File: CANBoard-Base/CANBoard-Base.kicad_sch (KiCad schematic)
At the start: 9 parts, among them J1 DTM12 A, J2 DTM12 B, U1 CANBoard, U8 LD1117S33CTR

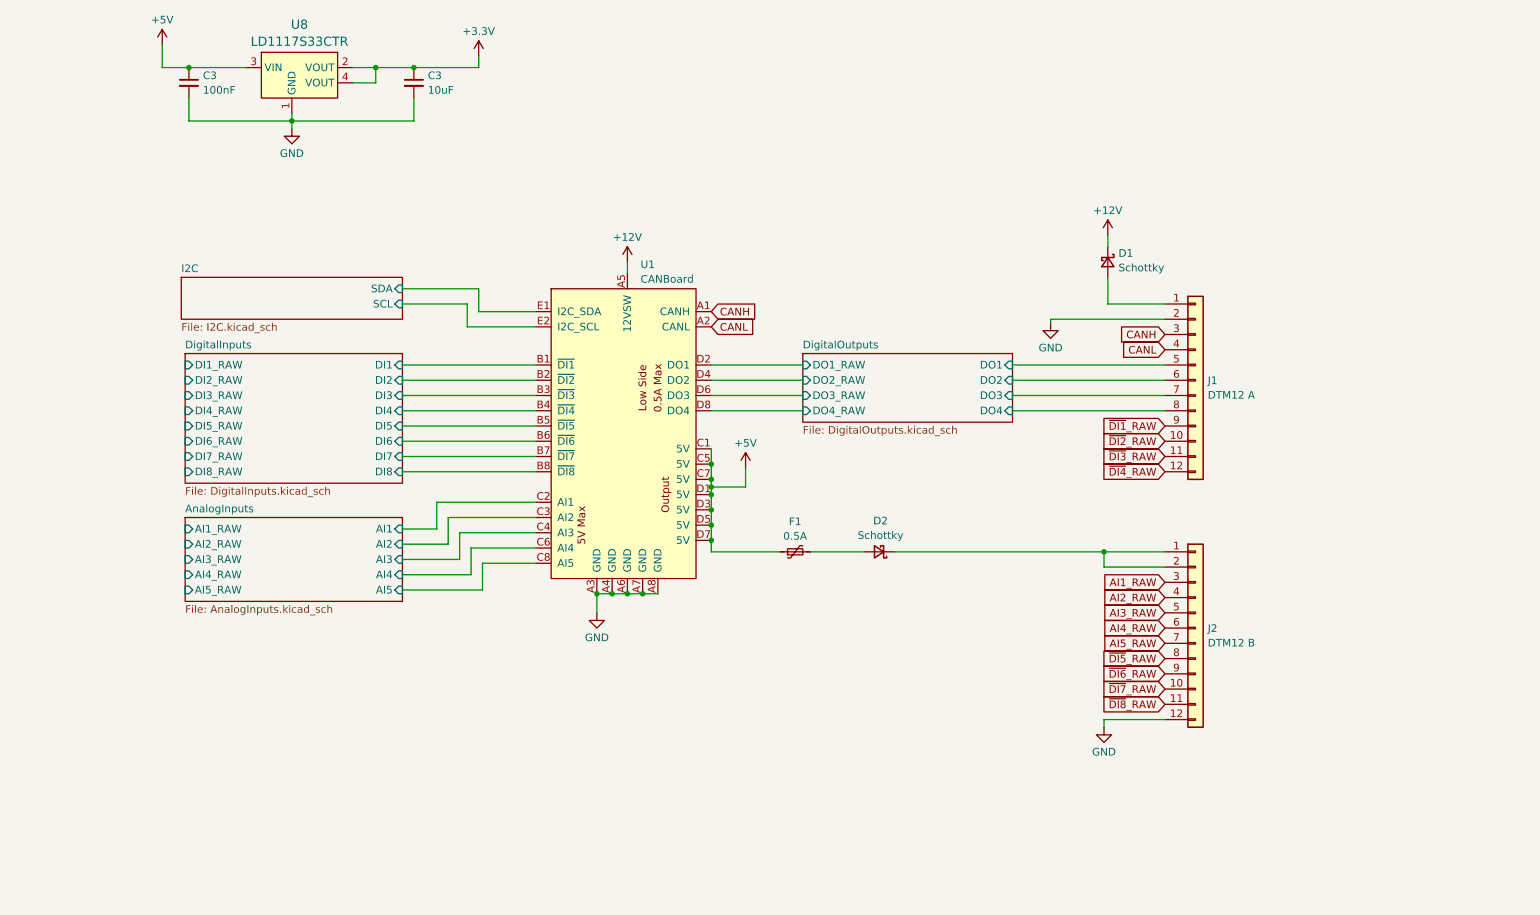
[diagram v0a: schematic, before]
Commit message: Switched to v2
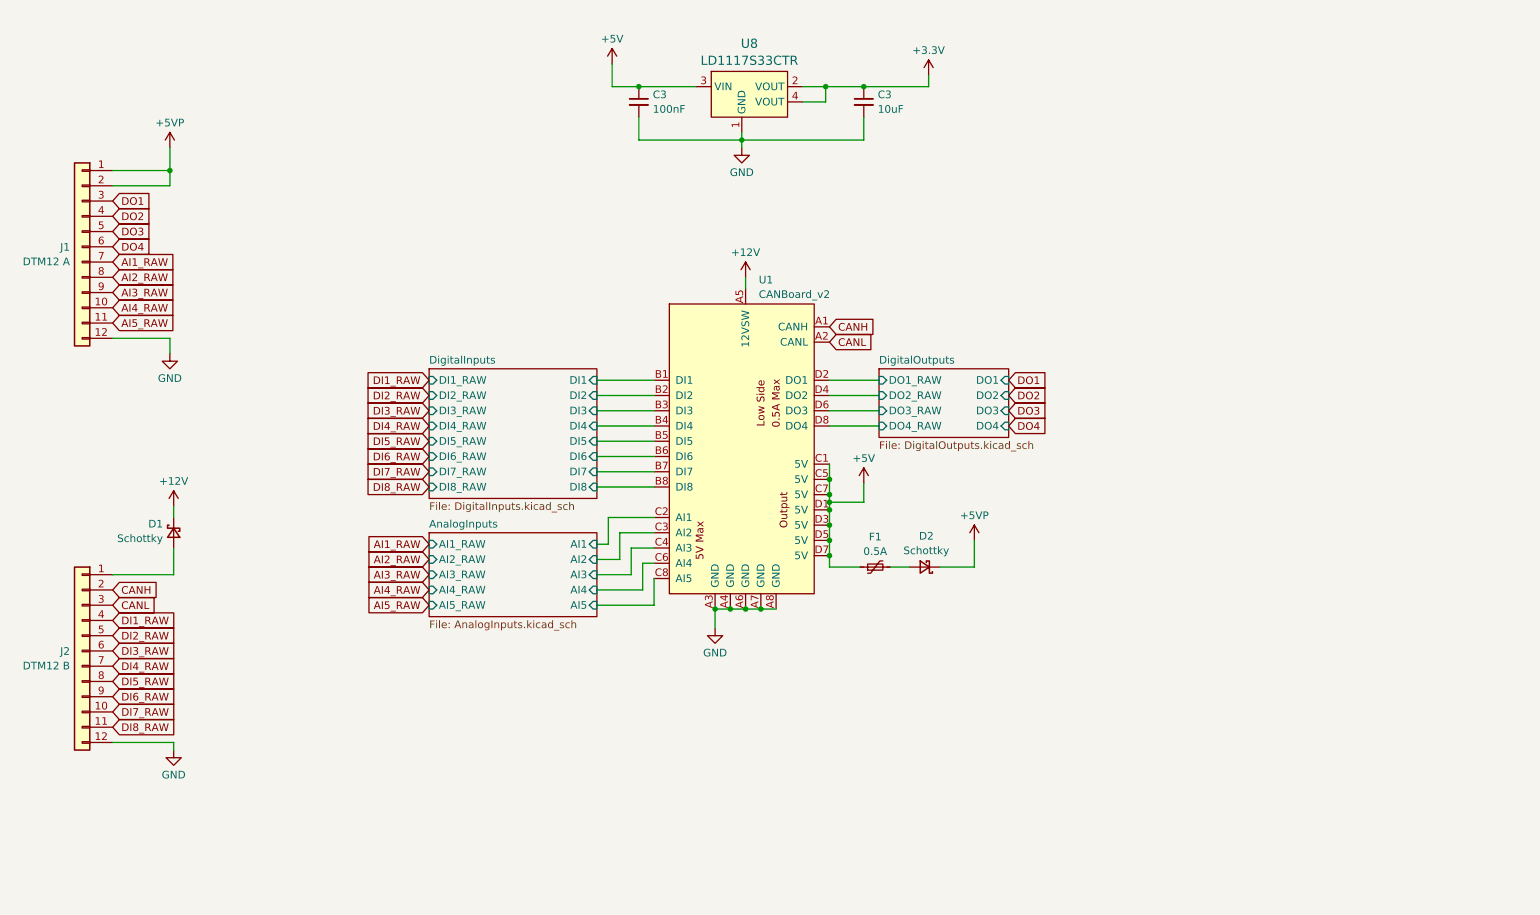
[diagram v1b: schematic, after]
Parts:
- D1, D2: footprint (none) -> Diode_SMD:D_SOD-123
- F1: footprint (none) -> Fuse:Fuse_0805_2012Metric
- J1, J2: footprint (none) -> Deutsch_DTM:TE_DTM15-12PA
- U1: value CANBoard -> CANBoard_v2; footprint CANBoard:CANBoard_v1 -> CANBoard:CANBoard_v2_NoMountingHoles; symbol CANBoard:CANBoard -> CANBoard:CANBoard_v2
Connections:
- net DigitalOutputs/DO3 is gone; now on net AI1_RAW: J1.7 (Pin_7)
- net DigitalOutputs/DO4 is gone; now on net AI2_RAW: J1.8 (Pin_8)
- net ~{DI1}_RAW is gone; now on net AI3_RAW: J1.9 (Pin_9)
- net ~{DI2}_RAW is gone; now on net AI4_RAW: J1.10 (Pin_10)
- net ~{DI3}_RAW is gone; now on net AI5_RAW: J1.11 (Pin_11)
- net ~{DI4}_RAW is gone; now on net GND: J1.12 (Pin_12)
- net AI1_RAW: no longer J2.3 (Pin_3)
- net AI2_RAW: no longer J2.4 (Pin_4)
- net AI3_RAW: no longer J2.5 (Pin_5)
- net AI4_RAW: no longer J2.6 (Pin_6)
- net AI5_RAW: no longer J2.7 (Pin_7)
- net CANH: now also J2.2 (Pin_2); no longer J1.3 (Pin_3)
- net CANL: now also J2.3 (Pin_3); no longer J1.4 (Pin_4)
- net GND: no longer J1.2 (Pin_2)
- net at D1.2 (A): now also J2.1 (Pin_1); no longer J1.1 (Pin_1)
- net DigitalOutputs/DO1 renamed DO3
- net DigitalOutputs/DO2 renamed DO4
- removed net I2C/SCL: U1.E2 (I2C_SCL)
- removed net I2C/SDA: U1.E1 (I2C_SDA)
- net ~{DI5}_RAW renamed DI5_RAW
- net ~{DI6}_RAW renamed DI6_RAW
- net ~{DI7}_RAW renamed DI7_RAW
- net ~{DI8}_RAW renamed DI8_RAW
- new net +5VP: D2.1 (K), J1.1 (Pin_1), J1.2 (Pin_2)
- new net DI1_RAW: J2.4 (Pin_4)
- new net DI2_RAW: J2.5 (Pin_5)
- new net DI3_RAW: J2.6 (Pin_6)
- new net DI4_RAW: J2.7 (Pin_7)
- new net DO1: J1.3 (Pin_3)
- new net DO2: J1.4 (Pin_4)
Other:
- removed sheet I2C
- moved on the sheet: C3, D1, D2, F1, J1, J2, U8

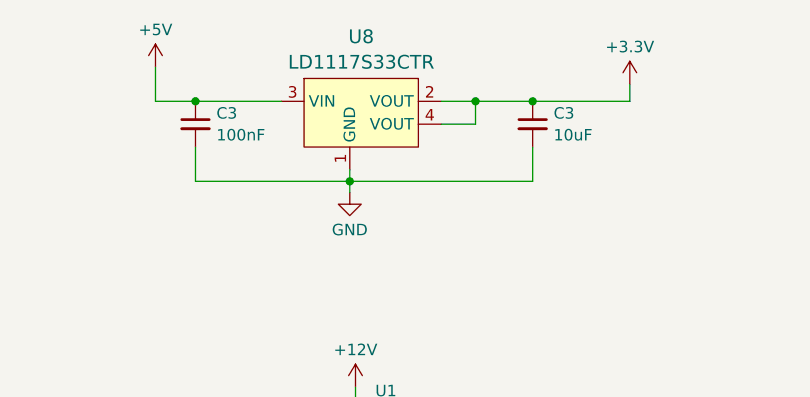
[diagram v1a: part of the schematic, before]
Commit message: Update to Kicad 8
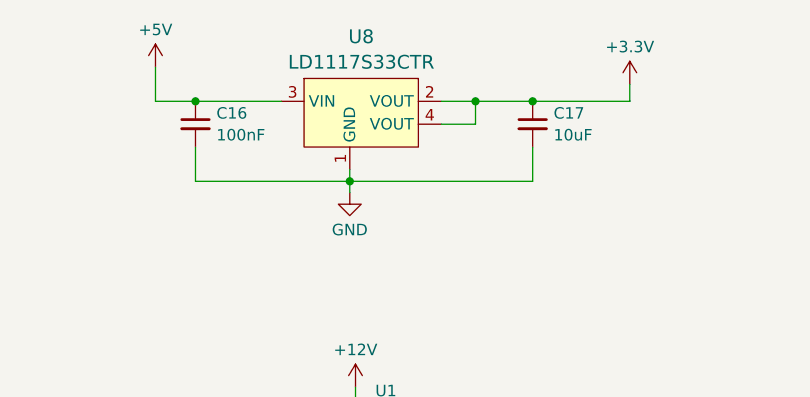
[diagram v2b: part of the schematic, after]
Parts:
- renumbered C3 to C16, C3 to C17

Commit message: first layout complete
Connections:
- net +5V: no longer U1.C5 (5V), U1.D3 (5V), U1.D5 (5V), U1.D7 (5V)
- net +5VP: now also J1.5 (Pin_5), J1.6 (Pin_6); no longer J1.1 (Pin_1), J1.2 (Pin_2)
- net CANH: now also J2.11 (Pin_11); no longer J2.2 (Pin_2)
- net CANL: now also J2.12 (Pin_12); no longer J2.3 (Pin_3)
- net DI1_RAW: now also J2.7 (Pin_7); no longer J2.4 (Pin_4)
- net DI2_RAW: now also J2.6 (Pin_6); no longer J2.5 (Pin_5)
- net DI3_RAW: now also J2.5 (Pin_5); no longer J2.6 (Pin_6)
- net DI4_RAW: now also J2.8 (Pin_8); no longer J2.7 (Pin_7)
- net DI5_RAW: now also J2.9 (Pin_9); no longer J2.8 (Pin_8)
- net DI6_RAW: now also J2.4 (Pin_4); no longer J2.9 (Pin_9)
- net DI7_RAW: now also J2.3 (Pin_3); no longer J2.10 (Pin_10)
- net DI8_RAW: now also J2.10 (Pin_10); no longer J2.11 (Pin_11)
- net DO1: now also J1.4 (Pin_4); no longer J1.3 (Pin_3)
- net DO2: now also J1.3 (Pin_3); no longer J1.4 (Pin_4)
- net DO3: now also J1.2 (Pin_2); no longer J1.5 (Pin_5)
- net DO4: now also J1.1 (Pin_1); no longer J1.6 (Pin_6)
- net GND: now also J2.2 (Pin_2); no longer J2.12 (Pin_12)
- no-connect marks 0 -> 4
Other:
- moved on the sheet: D2, F1, U1

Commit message: as built v1
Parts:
- added G1: DingoFace, DRTLogo:DingoFaceNoFill, symbol DRT_Logo:DRT_Logo
- C16: JLC_PN (none) -> C49678
- C17: JLC_PN (none) -> C15850
- D1, D2: JLC_PN (none) -> C179426
- F1: JLC_PN (none) -> C22378359
- J1, J2: now left out of the parts list
- U1: footprint CANBoard:CANBoard_v2_NoMountingHoles -> CANBoard:CANBoard_v2_TagConnectHoles; now left out of the parts list
- U8: JLC_PN (none) -> C35879
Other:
- moved on the sheet: D2
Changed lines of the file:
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@@
+	(wire
+		(pts
+			(xy 180.34 100.33) (xy 181.61 100.33)
+		)
+		(stroke
+			(width 0)
+			(type default)
+		)
+	)
 	(wire
 		(pts
@@
 	(wire
 		(pts
-			(xy 187.325 100.33) (xy 193.04 100.33)
-		)
-		(stroke
-			(width 0)
-			(type default)
-		)
-	)
-	(wire
-		(pts
 			(xy 130.175 113.03) (xy 137.795 113.03)
 		)
@@
 	(wire
 		(pts
+			(xy 49.53 66.04) (xy 50.8 66.04)
+		)
+		(stroke
+			(width 0)
+			(type default)
+		)
+	)
+	(wire
+		(pts
 			(xy 168.91 78.74) (xy 177.165 78.74)
 		)
@@
 	(wire
 		(pts
+			(xy 49.53 58.42) (xy 50.8 58.42)
+		)
+		(stroke
+			(width 0)
+			(type default)
+		)
+	)
+	(wire
+		(pts
 			(xy 130.175 81.28) (xy 139.7 81.28)
 		)
@@
 	(wire
 		(pts
+			(xy 49.53 63.5) (xy 50.8 63.5)
+		)
+		(stroke
+			(width 0)
+			(type default)
+		)
+	)
+	(wire
+		(pts
 			(xy 132.715 29.21) (xy 137.16 29.21)
 		)
@@
 	(wire
 		(pts
+			(xy 49.53 68.58) (xy 50.8 68.58)
+		)
+		(stroke
+			(width 0)
+			(type default)
+		)
+	)
+	(wire
+		(pts
 			(xy 130.175 115.57) (xy 139.7 115.57)
 		)
@@
 	(wire
 		(pts
-			(xy 180.34 100.33) (xy 182.245 100.33)
+			(xy 186.69 100.33) (xy 193.04 100.33)
 		)
 		(stroke
@@
 	(wire
 		(pts
+			(xy 49.53 60.96) (xy 50.8 60.96)
+		)
+		(stroke
+			(width 0)
+			(type default)
+		)
+	)
+	(wire
+		(pts
 			(xy 168.91 86.36) (xy 177.165 86.36)
 		)
@@
 	(global_label "AI2_RAW"
 		(shape input)
-		(at 49.53 60.96 0)
+		(at 50.8 60.96 0)
 		(fields_autoplaced yes)
 		(effects
@@
 		)
 		(property "Intersheetrefs" "${INTERSHEET_REFS}"
-			(at 60.1957 60.96 0)
+			(at 61.4657 60.96 0)
 			(effects
 				(font
@@
 	(global_label "AI5_RAW"
 		(shape input)
-		(at 49.53 68.58 0)
+		(at 50.8 68.58 0)
 		(fields_autoplaced yes)
 		(effects
@@
 		)
 		(property "Intersheetrefs" "${INTERSHEET_REFS}"
-			(at 60.1957 68.58 0)
+			(at 61.4657 68.58 0)
 			(effects
 				(font
@@
 	(global_label "AI1_RAW"
 		(shape input)
-		(at 49.53 58.42 0)
+		(at 50.8 58.42 0)
 		(fields_autoplaced yes)
 		(effects
@@
 		)
 		(property "Intersheetrefs" "${INTERSHEET_REFS}"
-			(at 60.1957 58.42 0)
+			(at 61.4657 58.42 0)
 			(effects
 				(font
@@
 	(global_label "AI4_RAW"
 		(shape input)
-		(at 49.53 66.04 0)
+		(at 50.8 66.04 0)
 		(fields_autoplaced yes)
 		(effects
@@
 		)
 		(property "Intersheetrefs" "${INTERSHEET_REFS}"
-			(at 60.1957 66.04 0)
+			(at 61.4657 66.04 0)
 			(effects
 				(font
@@
 	(global_label "AI3_RAW"
 		(shape input)
-		(at 49.53 63.5 0)
+		(at 50.8 63.5 0)
 		(fields_autoplaced yes)
 		(effects
@@
 		)
 		(property "Intersheetrefs" "${INTERSHEET_REFS}"
-			(at 60.1957 63.5 0)
+			(at 61.4657 63.5 0)
 			(effects
 				(font
@@
 			)
 		)
+		(property "JLC_PN" "C15850"
+			(at 174.625 31.75 0)
+			(effects
+				(font
+					(size 1.27 1.27)
+				)
+				(hide yes)
+			)
+		)
 		(pin "1"
 		)
@@
 		)
 		(property "Description" ""
+			(at 177.8 100.33 0)
+			(effects
+				(font
+					(size 1.27 1.27)
+				)
+				(hide yes)
+			)
+		)
+		(property "JLC_PN" "C22378359"
 			(at 177.8 100.33 0)
 			(effects
@@
 		(unit 1)
 		(exclude_from_sim no)
-		(in_bom yes)
+		(in_bom no)
 		(on_board yes)
 		(dnp no)
@@
 		)
 		(property "Description" ""
+			(at 44.45 55.88 0)
+			(effects
+				(font
+					(size 1.27 1.27)
+				)
+				(hide yes)
+			)
+		)
+		(property "JLC_PN" ""
 			(at 44.45 55.88 0)
 			(effects
@@
 		)
 		(property "Description" ""
+			(at 137.16 31.75 0)
+			(effects
+				(font
+					(size 1.27 1.27)
+				)
+				(hide yes)
+			)
+		)
+		(property "JLC_PN" "C49678"
 			(at 137.16 31.75 0)
 			(effects
@@
 			)
 		)
+		(property "JLC_PN" "C179426"
+			(at 59.69 103.505 0)
+			(effects
+				(font
+					(size 1.27 1.27)
+				)
+				(hide yes)
+			)
+		)
 		(pin "1"
 		)
@@
 	)
 	(symbol
+		(lib_id "DRT_Logo:DRT_Logo")
+		(at 273.05 162.56 0)
+		(unit 1)
+		(exclude_from_sim no)
+		(in_bom yes)
+		(on_board yes)
+		(dnp no)
+		(fields_autoplaced yes)
+		(property "Reference" "G1"
+			(at 273.685 161.3478 0)
+			(effects
+				(font
+					(size 1.27 1.27)
+				)
+				(justify left)
+			)
+		)
+		(property "Value" "DingoFace"
+			(at 273.685 163.7721 0)
+			(effects
+				(font
+					(size 1.27 1.27)
+				)
+				(justify left)
+			)
+		)
+		(property "Footprint" "DRTLogo:DingoFaceNoFill"
+			(at 273.05 162.56 0)
+			(effects
+				(font
+					(size 1.27 1.27)
+				)
+				(hide yes)
+			)
+		)
+		(property "Datasheet" ""
+			(at 273.05 162.56 0)
+			(effects
+				(font
+					(size 1.27 1.27)
+				)
+				(hide yes)
+			)
+		)
+		(property "Description" ""
+			(at 273.05 162.56 0)
+			(effects
+				(font
+					(size 1.27 1.27)
+				)
+				(hide yes)
+			)
+		)
+		(property "JLC_PN" ""
+			(at 273.05 162.56 0)
+			(effects
+				(font
+					(size 1.27 1.27)
+				)
+				(hide yes)
+			)
+		)
+		(instances
+			(project ""
+				(path "/ae3e8b14-da7b-493c-bdec-064ae45bef7a"
+					(reference "G1")
+					(unit 1)
+				)
+			)
+		)
+	)
+	(symbol
 		(lib_id "Connector_Generic:Conn_01x12")
 		(at 44.45 123.19 0)
@@
 		(unit 1)
 		(exclude_from_sim no)
-		(in_bom yes)
+		(in_bom no)
 		(on_board yes)
 		(dnp no)
@@
 		)
 		(property "Description" ""
+			(at 44.45 123.19 0)
+			(effects
+				(font
+					(size 1.27 1.27)
+				)
+				(hide yes)
+			)
+		)
+		(property "JLC_PN" ""
 			(at 44.45 123.19 0)
 			(effects
@@
 	(symbol
 		(lib_id "Device:D_Schottky_Small")
-		(at 184.785 100.33 180)
+		(at 184.15 100.33 180)
 		(unit 1)
 		(exclude_from_sim no)
@@
 		(fields_autoplaced yes)
 		(property "Reference" "D2"
-			(at 185.039 95.1697 0)
+			(at 184.404 95.1697 0)
 			(effects
 				(font
@@
 		)
 		(property "Value" "Schottky"
-			(at 185.039 97.5939 0)
+			(at 184.404 97.5939 0)
 			(effects
 				(font
@@
 		)
 		(property "Footprint" "Diode_SMD:D_SOD-123"
-			(at 184.785 100.33 90)
+			(at 184.15 100.33 90)
 			(effects
 				(font
@@
 		)
 		(property "Datasheet" "~"
-			(at 184.785 100.33 90)
+			(at 184.15 100.33 90)
 			(effects
 				(font
@@
 		)
 		(property "Description" ""
-			(at 184.785 100.33 0)
+			(at 184.15 100.33 0)
+			(effects
+				(font
+					(size 1.27 1.27)
+				)
+				(hide yes)
+			)
+		)
+		(property "JLC_PN" "C179426"
+			(at 184.15 100.33 0)
 			(effects
 				(font
@@
 			)
 		)
+		(property "JLC_PN" "C35879"
+			(at 154.305 29.21 0)
+			(effects
+				(font
+					(size 1.27 1.27)
+				)
+				(hide yes)
+			)
+		)
 		(pin "1"
 		)
@@
 		(unit 1)
 		(exclude_from_sim no)
-		(in_bom yes)
+		(in_bom no)
 		(on_board yes)
 		(dnp no)
@@
 			)
 		)
-		(property "Footprint" "CANBoard:CANBoard_v2_NoMountingHoles"
+		(property "Footprint" "CANBoard:CANBoard_v2_TagConnectHoles"
 			(at 123.19 69.85 0)
 			(effects
@@
 			(at 154.94 88.9 0)
 			(effects
+				(font
+					(size 1.27 1.27)
+				)
+				(hide yes)
+			)
+		)
+		(property "JLC_PN" ""
+			(at 154.94 88.9 0)
+			(effects

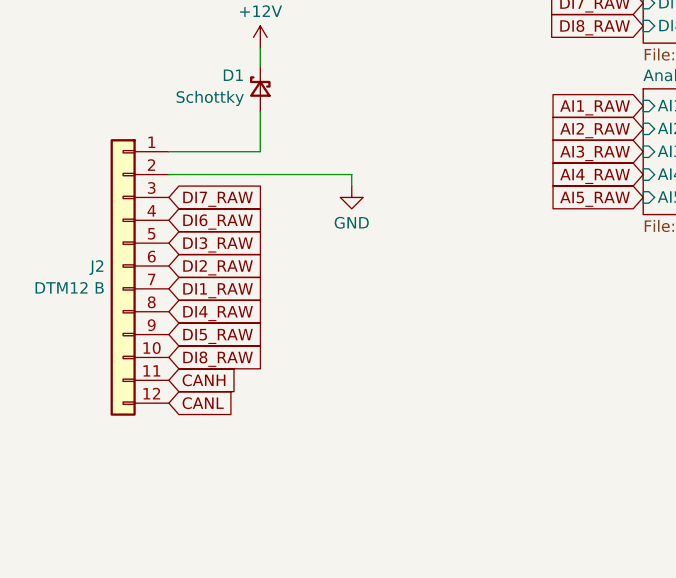
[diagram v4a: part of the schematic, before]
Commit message: moved dtm connectors together
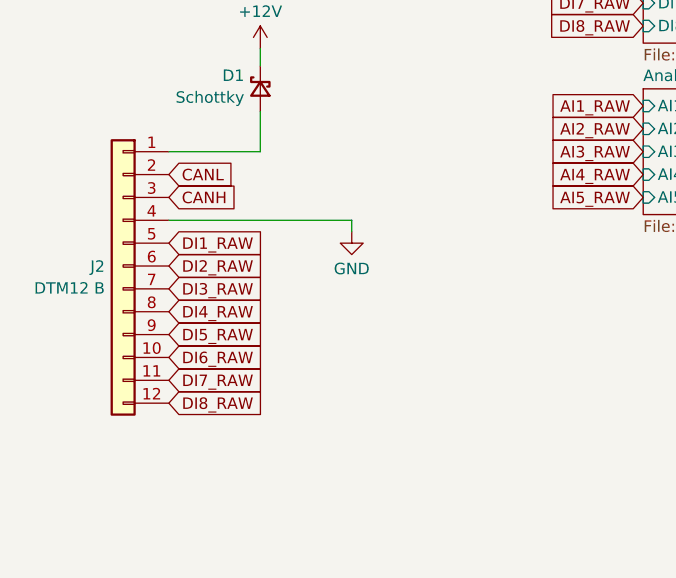
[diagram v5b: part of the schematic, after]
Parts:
- J1, J2: footprint Deutsch_DTM:TE_DTM15-12PA -> Deutsch_DTM:TE_DTM15-12Px_NoScrewHoles
- U1: footprint CANBoard:CANBoard_v2_TagConnectHoles -> CANBoard:CANBoard_v2_NoMountingHoles_TagConnectHoles
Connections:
- net CANH: now also J2.3 (Pin_3); no longer J2.11 (Pin_11)
- net CANL: now also J2.2 (Pin_2); no longer J2.12 (Pin_12)
- net DI1_RAW: now also J2.5 (Pin_5); no longer J2.7 (Pin_7)
- net DI3_RAW: now also J2.7 (Pin_7); no longer J2.5 (Pin_5)
- net DI6_RAW: now also J2.10 (Pin_10); no longer J2.4 (Pin_4)
- net DI7_RAW: now also J2.11 (Pin_11); no longer J2.3 (Pin_3)
- net DI8_RAW: now also J2.12 (Pin_12); no longer J2.10 (Pin_10)
- net GND: now also J2.4 (Pin_4); no longer J2.2 (Pin_2)

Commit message: added case
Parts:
- J1: Digi-Key_PN (none) -> DTM15-12PA
- J2: Digi-Key_PN (none) -> DTM15-12PB
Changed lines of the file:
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@@
+			)
+		)
+		(property "Digi-Key_PN" "DTM15-12PA"
+			(at 44.45 55.88 0)
+			(effects
+				(font
+					(size 1.27 1.27)
+				)
+				(hide yes)
 			)
 		)
@@
 			(at 44.45 123.19 0)
 			(effects
+				(font
+					(size 1.27 1.27)
+				)
+				(hide yes)
+			)
+		)
+		(property "Digi-Key_PN" "DTM15-12PB"
+			(at 44.45 123.19 0)
+			(effects
